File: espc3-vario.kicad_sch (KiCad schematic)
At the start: 54 parts, among them J1 conn_pgm, J2 conn_bat, J3 USB_C_6PIN, Q1 AO3401A, Q2 2N7002, SW1 RST, SW2 PCC, SW3 PWR, U1 CJMCU-117, U2 ESPC3-12F C3FN4, U3 TLV75533PDBV, U4 74HC240PWR, U5 MCP73831-2-OT

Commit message: update
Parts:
- C1, C10, C12, C13, C2, C4, C7: LCSC (none) -> C49678
- C11, C14, C15, C8, C9: LCSC (none) -> C5672
- C3: LCSC (none) -> C28323
- C5, C6: LCSC (none) -> C15008
- D1: LCSC (none) -> C191023
- D2: LCSC (none) -> C189307
- D3: LCSC (none) -> C51125
- D4: LCSC (none) -> C138549
- F1: LCSC (none) -> C70078
- L1, L2: LCSC (none) -> C1017
- Q1: LCSC (none) -> C15127
- Q2: LCSC (none) -> C8545
- R1, R5: LCSC (none) -> C17530
- R10, R12, R2, R3, R4, R7, R8, R9: LCSC (none) -> C17724
- R11, R13: value 5K1 -> 5K1 1%; LCSC (none) -> C27834
- R14, R15, R6: LCSC (none) -> C17520
- R16: LCSC (none) -> C17604
- U3: LCSC (none) -> C404027
- U4: LCSC (none) -> C470968
- U5: LCSC (none) -> C424093

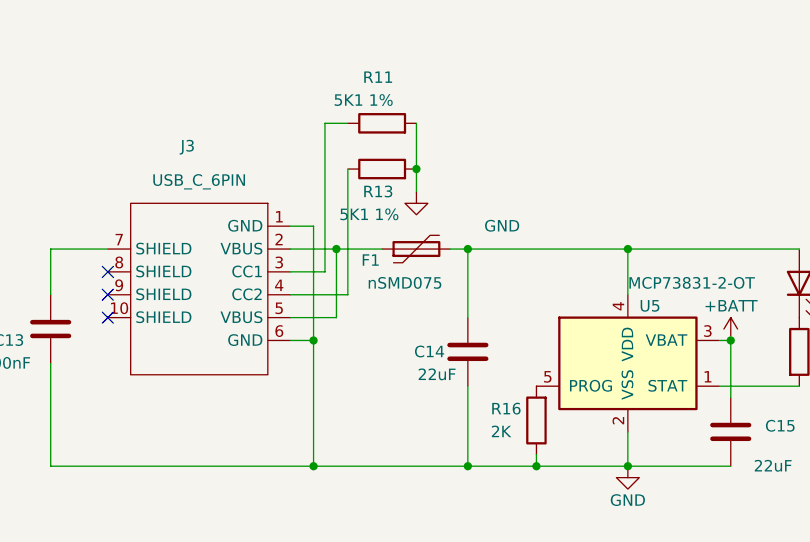
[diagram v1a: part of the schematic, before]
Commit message: change fuse
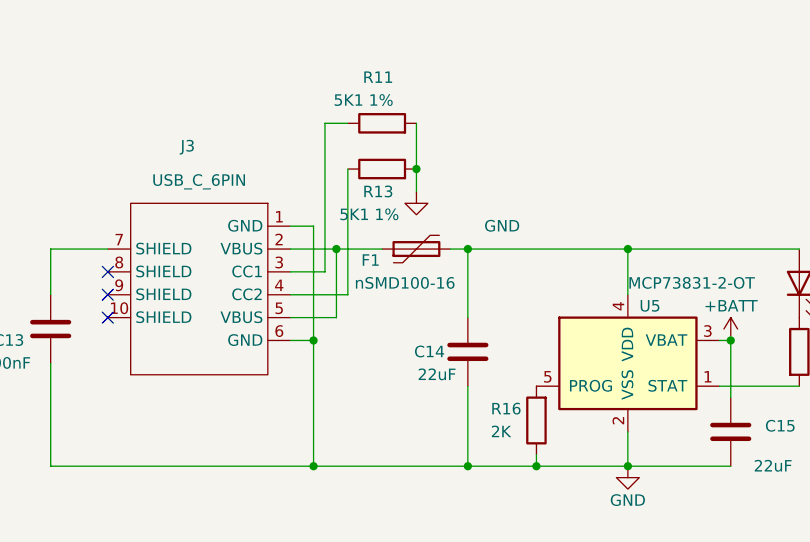
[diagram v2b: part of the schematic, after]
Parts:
- F1: value nSMD075 -> nSMD100-16
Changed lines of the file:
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@@
       (effects (font (size 1.27 1.27)))
     )
-    (property "Value" "nSMD075" (id 1) (at 124.46 156.21 90)
+    (property "Value" "nSMD100-16" (id 1) (at 124.46 156.21 90)
       (effects (font (size 1.27 1.27)))
     )
@@
     )
     (path "/6f4bf812-138c-435a-8325-99bdfcb7fb2e"
-      (reference "F1") (unit 1) (value "nSMD075") (footprint "00_project_footprints:Fuse_1206_3216Metric_Pad1.42x1.75mm_HandSolder")
+      (reference "F1") (unit 1) (value "nSMD100-16") (footprint "00_project_footprints:Fuse_1206_3216Metric_Pad1.42x1.75mm_HandSolder")
     )
     (path "/cae03f2c-c8dd-473c-a40d-a521ec77da9a"
